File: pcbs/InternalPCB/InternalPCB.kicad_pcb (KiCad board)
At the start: 2 copper layers, 16 parts, among them J1 Conn_01x20, J10 694106301002, J2 Conn_01x20, J3 Conn_01x04_Pin, J4 Conn_01x04_Pin, J5 Conn_01x02_Pin, J6 Conn_01x04_Pin, J7 Conn_01x03_Pin, J8 Conn_01x05_Pin, J9 Conn_01x05_Pin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

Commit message: Innenmodul erstes funktionales PCB
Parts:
- moved U4 106.5 mm to (102.9, 130.7), turned to 180 degrees
- moved J9 103.1 mm to (53.3, 165.1), turned to 180 degrees
- moved J3 99.0 mm to (131.1, 126.2), turned to -90 degrees
- moved U3 98.2 mm to (86.8, 165.1)
- moved J4 98.2 mm to (131.1, 133.8), turned to -90 degrees
- moved J8 89.7 mm to (73.7, 154.9)
- moved U1 80.2 mm to (62.2, 119.5)
- moved U2 67.6 mm to (102.9, 118.1)
- moved J6 67.3 mm to (116.8, 81.3)
- moved J5 64.7 mm to (121.9, 101.6), turned to -90 degrees
- moved J7 63.7 mm to (116.8, 73.7), turned to 180 degrees
- moved SW1 61.4 mm to (32.3, 58.7)
- moved J2 57.4 mm to (53.3, 40.6)
- moved J10 48.7 mm to (24.6, 80.0)
- moved J1 40.1 mm to (71.1, 40.6)
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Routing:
- net +5V: track 0.00 -> 350.4 mm
- net PICO_RESET: track 0.00 -> 197.8 mm, vias 0 -> 2
- net SDIO_CLK: track 0.00 -> 158.0 mm
- net LCD_DC: track 0.00 -> 124.9 mm
- net LCD_CS: track 0.00 -> 116.5 mm
- net D2: track 0.00 -> 106.3 mm
- net CLK: track 0.00 -> 103.4 mm
- net D1: track 0.00 -> 98.3 mm
- net Net-(J7-Pin_2): track 0.00 -> 97.0 mm
- net 3.3V: track 0.00 -> 96.2 mm, vias 0 -> 1
- net MOSI: track 0.00 -> 95.4 mm
- net D0: track 0.00 -> 90.3 mm
- net MISO: track 0.00 -> 87.4 mm
- net SDIO_CMD: track 0.00 -> 82.3 mm
- net LCD_BL: track 0.00 -> 79.4 mm
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- added copper zone on B.Cu, net GND
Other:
- board outline added: 111.8 x 139.7 mm
- board text added: "3.3V"
- board text added: "5V"
- board text added: "BME280"
- board text added: "CAL"
- board text added: "CO2 CAL"
- board text added: "Display und RTC"
- board text added: "GND"
- board text added: "GUI Pico W"
- board text added: "HC-12"
- board text added: "HKW581"
- board text added: "HKW581 RST"
- board text added: "Innenmodul der Wetterstation WiSe 2023/2024 BU HAW Hamburg © Lasse Kelling, Fabian Schmalenbach Januar 2024"
- board text added: "MH-Z19C"
- board text added: "PWM"
- board text added: "RST"
- board text added: "RX"
- board text added: "SCL"
- board text added: "SDA"
- board text added: "SET"
- board text added: "Sensor Pico"
- board text added: "TX"
- board text added: "USB"

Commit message: 3,3V für RTC ausgeführt
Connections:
- J1 pad 5: unconnected-(J1-Pin_5-Pad5) -> 3.3V
- U1 pad 36: unconnected-(U1-3V3-Pad36) -> 3.3V
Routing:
- net 3.3V: track 96.2 -> 194.9 mm, vias 1 -> 2

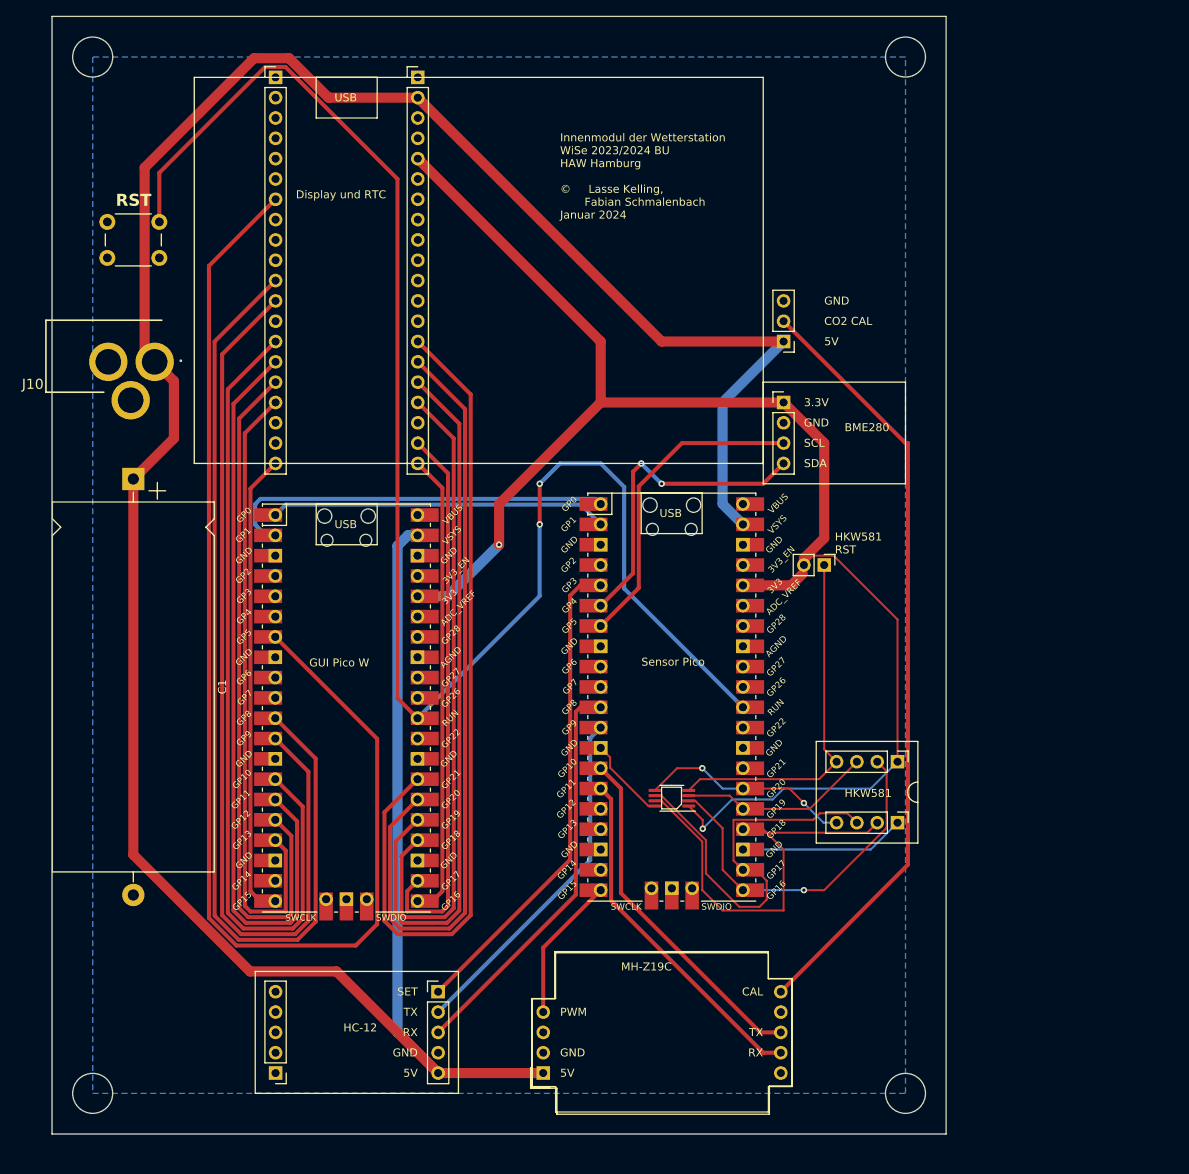
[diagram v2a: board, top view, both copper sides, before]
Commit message: PCB Innenmodul verbessert
- Löcher für Displaymontage
- 2. Stromanschluss für Wandmontage
- M3 Löcher für Gehäuse und Wandmontage
- Beschriftung angepasst
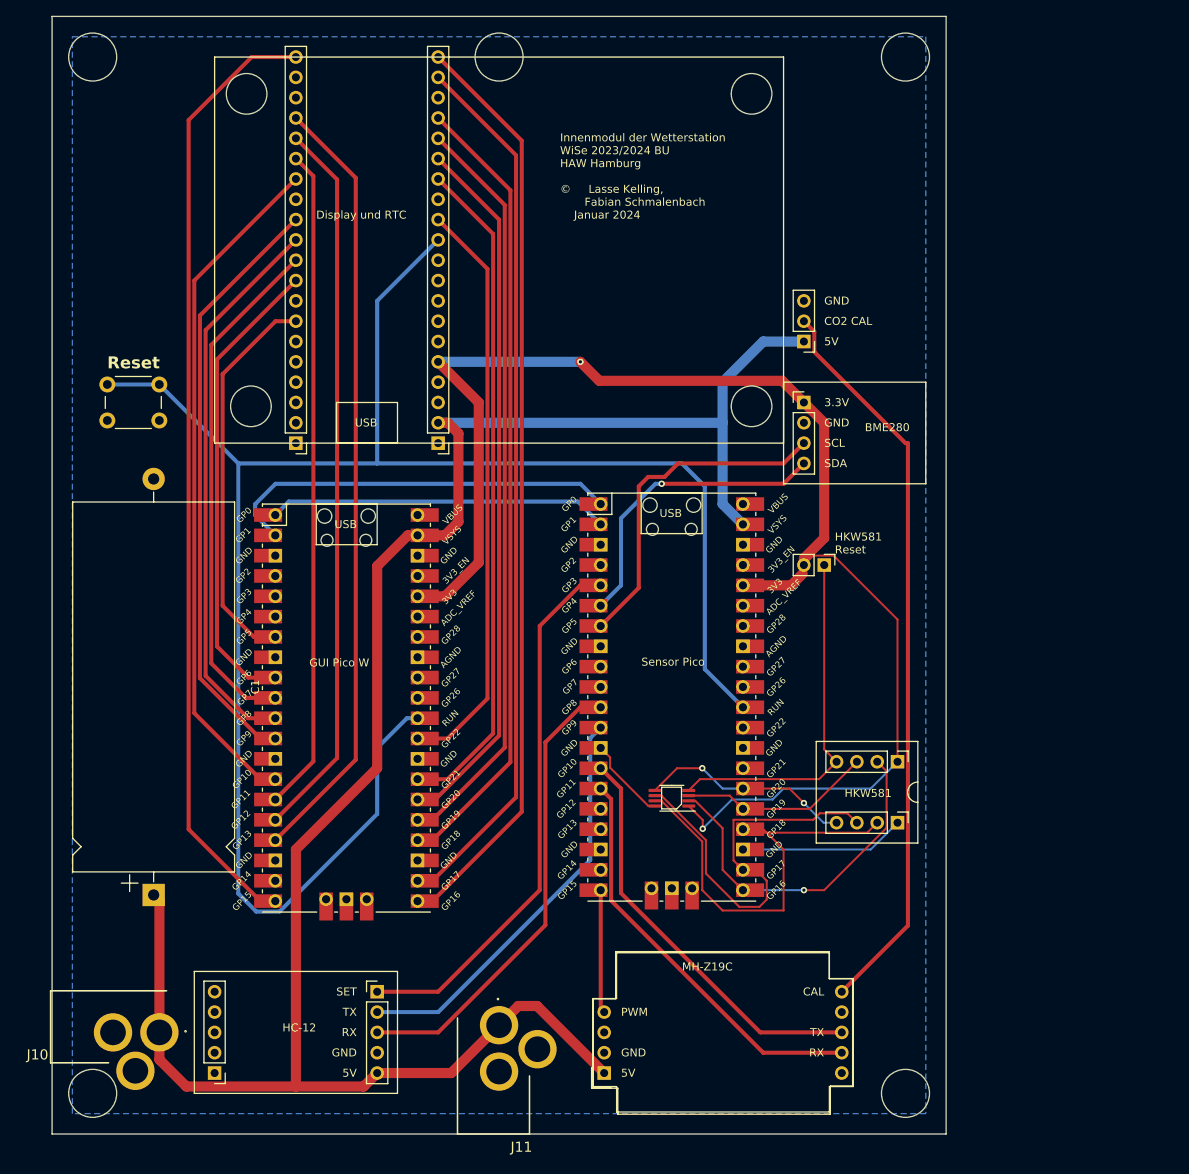
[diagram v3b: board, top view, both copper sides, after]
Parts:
- added J11: 694106301002, 694106301002:694106301002_1, F.Cu at (85.1, 172.7)
- moved J10 83.8 mm to (25.2, 163.8)
- moved C1 52.1 mm to (38.1, 142.8), turned to 90 degrees
- moved J1 45.8 mm to (73.7, 86.4), turned to 180 degrees
- moved J2 45.8 mm to (55.9, 86.4), turned to 180 degrees
- moved SW1 20.3 mm to (32.3, 79.0)
- moved J9 7.62 mm to (45.7, 165.1)
- moved U3 7.62 mm to (94.4, 165.1)
- moved J8 7.62 mm to (66.0, 154.9)
- moved J6 2.54 mm to (119.4, 81.3)
- moved J7 2.54 mm to (119.4, 73.7)
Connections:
- net D1 renamed D1 / RTC_SDA
- net D2 renamed D2 / RTC_SCL
- J1 pad 11: unconnected-(J1-Pin_11-Pad11) -> PICO_RESET
- J2 pad 10: unconnected-(J2-Pin_10-Pad10) -> RTC_SCL_ALT
- J2 pad 9: unconnected-(J2-Pin_9-Pad9) -> RTC_SDA_ALT
- U1 pad 10: unconnected-(U1-GPIO7-Pad10) -> RTC_SCL_ALT
- U1 pad 9: unconnected-(U1-GPIO6-Pad9) -> RTC_SDA_ALT
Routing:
- net SDIO_CLK: track 158.0 -> 49.0 mm
- net +5V: track 350.4 -> 248.0 mm
- net DC_CS/D3: track 0.00 -> 73.2 mm
- net RTC_SCL_ALT: track 0.00 -> 64.6 mm
- net LCD_RST: track 58.4 -> 119.9 mm
- net RTC_SDA_ALT: track 0.00 -> 58.7 mm
- net TP_CS: track 58.4 -> 116.3 mm
- net LCD_DC: track 124.9 -> 70.1 mm
- net LCD_CS: track 116.5 -> 74.8 mm
- net TP_IRQ: track 69.2 -> 110.7 mm
- net PICO_RESET: track 197.8 -> 232.6 mm, vias 2 -> 0
- net D2 / RTC_SCL: track 106.3 -> 84.0 mm
- net LCD_BL: track 79.4 -> 97.5 mm
- net CLK: track 103.4 -> 85.6 mm
- net SDIO_CMD: track 82.3 -> 99.9 mm
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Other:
- outline, holes or cut-outs redrawn
- board text added: "HKW581 Reset"
- board text added: "Reset"
- board text removed: "HKW581 RST"
- board text removed: "RST"

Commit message: Elko footprint getauscht
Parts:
- C1: footprint Capacitor_THT:CP_Axial_L46.0mm_D20.0mm_P52.00mm_Horizontal -> Capacitor_THT:C_Radial_D10.0mm_H16.0mm_P5.00mm
- moved C1 4.55 mm to (36.3, 147.0)
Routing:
- net +5V: track 248.0 -> 244.6 mm
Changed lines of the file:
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@@
     )
   )
-  (footprint "Capacitor_THT:CP_Axial_L46.0mm_D20.0mm_P52.00mm_Horizontal" (layer "F.Cu")
-    (at 38.1 142.84 90)
-    (descr "CP, Axial series, Axial, Horizontal, pin pitch=52mm, , length*diameter=46*20mm^2, Electrolytic Capacitor")
-    (tags "CP Axial series Axial Horizontal pin pitch 52mm  length 46mm diameter 20mm Electrolytic Capacitor")
+  (footprint "Capacitor_THT:C_Radial_D10.0mm_H16.0mm_P5.00mm" (layer "F.Cu")
+    (at 36.322 147.026 90)
+    (descr "C, Radial series, Radial, pin pitch=5.00mm, diameter=10mm, height=16mm, Non-Polar Electrolytic Capacitor")
+    (tags "C Radial series Radial pin pitch 5.00mm diameter 10mm height 16mm Non-Polar Electrolytic Capacitor")
     (property "Sheetfile" "InternalPCB.kicad_sch")
     (property "Sheetname" "")
@@
     (property "ki_keywords" "cap capacitor")
     (attr through_hole)
-    (fp_text reference "C1" (at 26 12.7 90) (layer "F.SilkS")
-        (effects (font (size 1 1) (thickness 0.15)))
-    )
-    (fp_text value "1000u" (at 26 11.12 90) (layer "F.Fab")
-        (effects (font (size 1 1) (thickness 0.15)))
-    )
-    (fp_text user "${REFERENCE}" (at 26 0 90) (layer "F.Fab")
-        (effects (font (size 1 1) (thickness 0.15)))
-    )
-    (fp_line (start 0.43 -3) (end 2.53 -3)
-      (stroke (width 0.12) (type solid)) (layer "F.SilkS"))
-    (fp_line (start 1.48 -4.05) (end 1.48 -1.95)
-      (stroke (width 0.12) (type solid)) (layer "F.SilkS"))
-    (fp_line (start 1.64 0) (end 2.88 0)
-      (stroke (width 0.12) (type solid)) (layer "F.SilkS"))
-    (fp_line (start 2.88 -10.12) (end 2.88 10.12)
-      (stroke (width 0.12) (type solid)) (layer "F.SilkS"))
-    (fp_line (start 2.88 -10.12) (end 4.98 -10.12)
-      (stroke (width 0.12) (type solid)) (layer "F.SilkS"))
-    (fp_line (start 2.88 10.12) (end 4.98 10.12)
-      (stroke (width 0.12) (type solid)) (layer "F.SilkS"))
-    (fp_line (start 4.98 -10.12) (end 6.03 -9.07)
-      (stroke (width 0.12) (type solid)) (layer "F.SilkS"))
-    (fp_line (start 4.98 10.12) (end 6.03 9.07)
-      (stroke (width 0.12) (type solid)) (layer "F.SilkS"))
-    (fp_line (start 6.03 -9.07) (end 7.08 -10.12)
-      (stroke (width 0.12) (type solid)) (layer "F.SilkS"))
-    (fp_line (start 6.03 9.07) (end 7.08 10.12)
-      (stroke (width 0.12) (type solid)) (layer "F.SilkS"))
-    (fp_line (start 7.08 -10.12) (end 49.12 -10.12)
-      (stroke (width 0.12) (type solid)) (layer "F.SilkS"))
-    (fp_line (start 7.08 10.12) (end 49.12 10.12)
-      (stroke (width 0.12) (type solid)) (layer "F.SilkS"))
-    (fp_line (start 49.12 -10.12) (end 49.12 10.12)
-      (stroke (width 0.12) (type solid)) (layer "F.SilkS"))
-    (fp_line (start 50.36 0) (end 49.12 0)
-      (stroke (width 0.12) (type solid)) (layer "F.SilkS"))
-    (fp_line (start -1.65 -10.25) (end -1.65 10.25)
-      (stroke (width 0.05) (type solid)) (layer "F.CrtYd"))
-    (fp_line (start -1.65 10.25) (end 53.65 10.25)
-      (stroke (width 0.05) (type solid)) (layer "F.CrtYd"))
-    (fp_line (start 53.65 -10.25) (end -1.65 -10.25)
-      (stroke (width 0.05) (type solid)) (layer "F.CrtYd"))
-    (fp_line (start 53.65 10.25) (end 53.65 -10.25)
-      (stroke (width 0.05) (type solid)) (layer "F.CrtYd"))
-    (fp_line (start 0 0) (end 3 0)
-      (stroke (width 0.1) (type solid)) (layer "F.Fab"))
-    (fp_line (start 3 -10) (end 3 10)
-      (stroke (width 0.1) (type solid)) (layer "F.Fab"))
-    (fp_line (start 3 -10) (end 4.98 -10)
-      (stroke (width 0.1) (type solid)) (layer "F.Fab"))
-    (fp_line (start 3 10) (end 4.98 10)
-      (stroke (width 0.1) (type solid)) (layer "F.Fab"))
-    (fp_line (start 4.98 -10) (end 6.03 -8.95)
-      (stroke (width 0.1) (type solid)) (layer "F.Fab"))
-    (fp_line (start 4.98 10) (end 6.03 8.95)
-      (stroke (width 0.1) (type solid)) (layer "F.Fab"))
-    (fp_line (start 5 0) (end 7.1 0)
-      (stroke (width 0.1) (type solid)) (layer "F.Fab"))
-    (fp_line (start 6.03 -8.95) (end 7.08 -10)
-      (stroke (width 0.1) (type solid)) (layer "F.Fab"))
-    (fp_line (start 6.03 8.95) (end 7.08 10)
-      (stroke (width 0.1) (type solid)) (layer "F.Fab"))
-    (fp_line (start 6.05 -1.05) (end 6.05 1.05)
-      (stroke (width 0.1) (type solid)) (layer "F.Fab"))
-    (fp_line (start 7.08 -10) (end 49 -10)
-      (stroke (width 0.1) (type solid)) (layer "F.Fab"))
-    (fp_line (start 7.08 10) (end 49 10)
-      (stroke (width 0.1) (type solid)) (layer "F.Fab"))
-    (fp_line (start 49 -10) (end 49 10)
-      (stroke (width 0.1) (type solid)) (layer "F.Fab"))
-    (fp_line (start 52 0) (end 49 0)
-      (stroke (width 0.1) (type solid)) (layer "F.Fab"))
-    (pad "1" thru_hole rect (at 0 0 90) (size 2.8 2.8) (drill 1.4) (layers "*.Cu" "*.Mask")
+    (fp_text reference "C1" (at 2.5 -6.25 90) (layer "F.SilkS")
+        (effects (font (size 1 1) (thickness 0.15)))
+    )
+    (fp_text value "1000u" (at 2.5 6.25 90) (layer "F.Fab")
+        (effects (font (size 1 1) (thickness 0.15)))
+    )
+    (fp_text user "${REFERENCE}" (at 2.5 0 90) (layer "F.Fab")
+        (effects (font (size 1 1) (thickness 0.15)))
+    )
+    (fp_circle (center 2.5 0) (end 7.62 0)
+      (stroke (width 0.12) (type solid)) (fill none) (layer "F.SilkS"))
+    (fp_circle (center 2.5 0) (end 7.75 0)
+      (stroke (width 0.05) (type solid)) (fill none) (layer "F.CrtYd"))
+    (fp_circle (center 2.5 0) (end 7.5 0)
+      (stroke (width 0.1) (type solid)) (fill none) (layer "F.Fab"))
+    (pad "1" thru_hole circle (at 0 0 90) (size 1.6 1.6) (drill 0.8) (layers "*.Cu" "*.Mask")
       (net 1 "+5V") (pintype "passive"))
-    (pad "2" thru_hole oval (at 52 0 90) (size 2.8 2.8) (drill 1.4) (layers "*.Cu" "*.Mask")
+    (pad "2" thru_hole circle (at 5 0 90) (size 1.6 1.6) (drill 0.8) (layers "*.Cu" "*.Mask")
       (net 2 "GND") (pintype "passive"))
-    (model "${KICAD6_3DMODEL_DIR}/Capacitor_THT.3dshapes/CP_Axial_L46.0mm_D20.0mm_P52.00mm_Horizontal.wrl"
+    (model "${KICAD6_3DMODEL_DIR}/Capacitor_THT.3dshapes/C_Radial_D10.0mm_H16.0mm_P5.00mm.wrl"
       (offset (xyz 0 0 0))
       (scale (xyz 1 1 1))
@@
     (effects (font (size 1 1) (thickness 0.15)) (justify left bottom))
   )
-  (segment (start 38.82 143.56) (end 38.1 142.84) (width 1.27) (layer "F.Cu") (net 1))
   (segment (start 76.2 96.202874) (end 74.515 97.887874) (width 1.27) (layer "F.Cu") (net 1))
   (segment (start 66.04 127) (end 55.88 137.16) (width 1.27) (layer "F.Cu") (net 1))
   (segment (start 66.04 165.1) (end 64.355 166.785) (width 1.27) (layer "F.Cu") (net 1))
-  (segment (start 38.82 160.02) (end 38.82 143.56) (width 1.27) (layer "F.Cu") (net 1))
   (segment (start 74.515 97.887874) (end 71.086695 97.887874) (width 1.27) (layer "F.Cu") (net 1))
   (segment (start 69.884614 97.887874) (end 66.04 101.732488) (width 1.27) (layer "F.Cu") (net 1))
   (segment (start 66.04 165.1) (end 75.3 165.1) (width 1.27) (layer "F.Cu") (net 1))
+  (segment (start 38.82 160.02) (end 38.82 149.524) (width 1.27) (layer "F.Cu") (net 1))
   (segment (start 73.66 83.82) (end 74.862081 83.82) (width 1.27) (layer "F.Cu") (net 1))
   (segment (start 42.190888 166.785) (end 38.82 163.414112) (width 1.27) (layer "F.Cu") (net 1))
@@
   (segment (start 64.355 166.785) (end 55.88 166.785) (width 1.27) (layer "F.Cu") (net 1))
   (segment (start 75.3 165.1) (end 81.28 159.12) (width 1.27) (layer "F.Cu") (net 1))
+  (segment (start 38.82 149.524) (end 36.322 147.026) (width 1.27) (layer "F.Cu") (net 1))
   (segment (start 38.82 163.414112) (end 38.82 160.02) (width 1.27) (layer "F.Cu") (net 1))
   (segment (start 81.28 159.12) (end 83.68 156.72) (width 1.27) (layer "F.Cu") (net 1))

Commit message: Bisschen DRC dies das
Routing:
- net Net-(J7-Pin_2): track 92.8 -> 94.6 mm
- net 3.3V: track 179.6 -> 178.6 mm
- net LCD_RST: track 119.9 -> 120.8 mm
- net CLK: track 85.6 -> 86.5 mm
- net HKW581_DOUT: track 51.4 -> 52.1 mm, vias 0 -> 2
- net LCD_CS: track 74.8 -> 75.4 mm
- net SDIO_CMD: track 99.9 -> 100.4 mm
- net Net-(J3-Pin_4): track 45.2 -> 45.3 mm, vias 0 -> 2
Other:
- board text added: "+"
- board text added: "."
